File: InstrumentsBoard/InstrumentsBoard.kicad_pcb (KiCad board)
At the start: 2 copper layers, 105.7 x 47.1 mm, 24 parts, among them J1 RJ45_LED_Shielded, Q1 BSS138, Q2 BSS138, U1 Teensy4.1_DEV-16771, U2 OKI

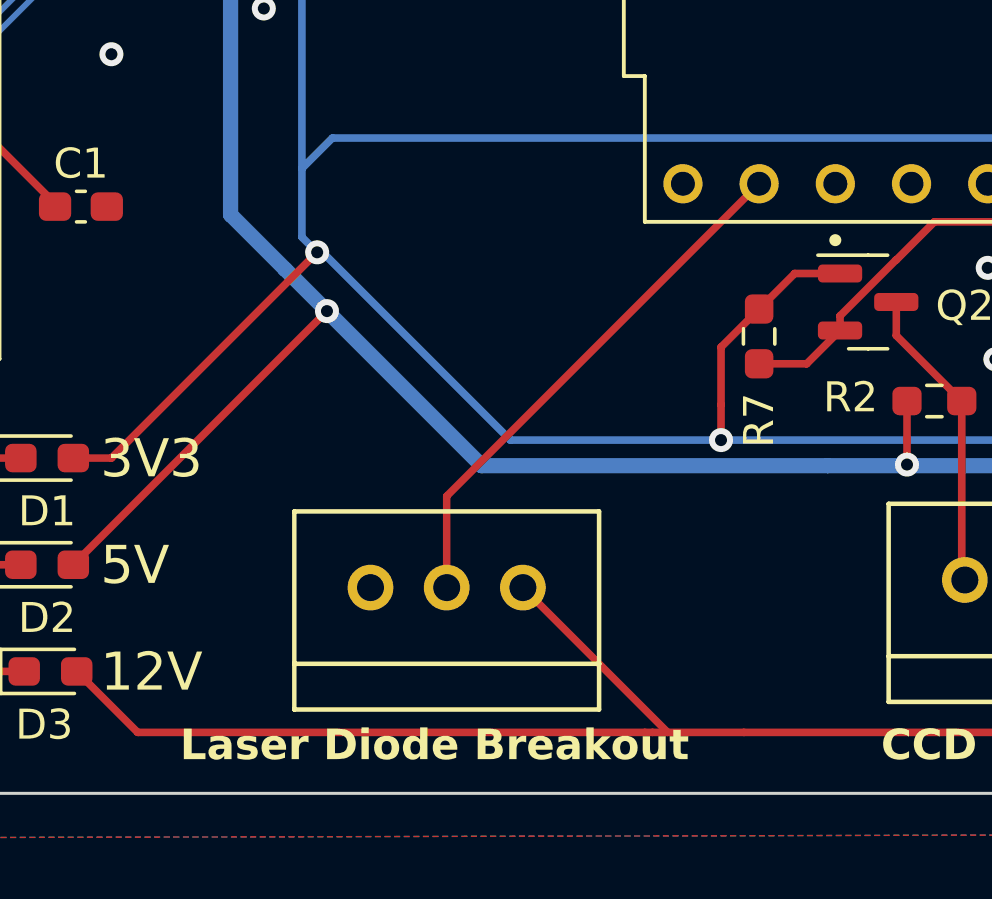
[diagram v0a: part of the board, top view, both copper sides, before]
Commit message: Revert "revert back to laser diode board"
This reverts commit 6528700a9c51bf2c3bc149a74fbf2f6639f4022b.
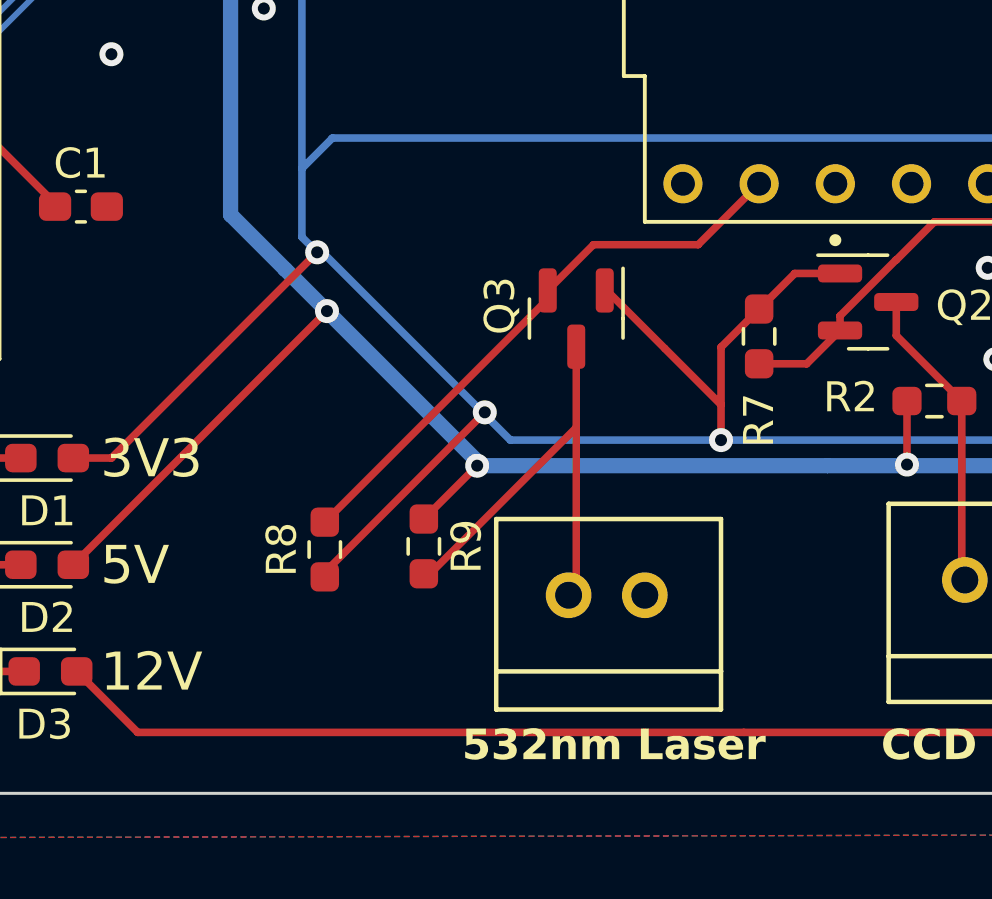
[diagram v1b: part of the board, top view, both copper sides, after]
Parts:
- removed Conn3: Molex_SL_03, MRDT_Connectors:MOLEX_SL_03_Vertical
- added Conn5: Molex_SL_02, MRDT_Connectors:MOLEX_SL_02_Vertical, F.Cu at (67.3, 67.3)
- added Q3: BSS138BK, Package_TO_SOT_SMD:SOT-23, F.Cu at (65.0, 58.1)
- added R8: 4.7k, Resistor_SMD:R_0603_1608Metric_Pad0.98x0.95mm_HandSolder, F.Cu at (56.6, 65.8)
- added R9: 4.7k, Resistor_SMD:R_0603_1608Metric_Pad0.98x0.95mm_HandSolder, F.Cu at (59.9, 65.7)
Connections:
- U1 pad 0: Green_LED -> Green_Laser_3V3
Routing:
- net Green_Laser_3V3: track 0.00 -> 19.3 mm
- net Green_LED: track 17.8 -> 0.00 mm
- net Green_Laser_5V: track 0.00 -> 15.5 mm
- net +3V3: track 139.7 -> 152.8 mm, vias 3 -> 4
- net +12V: track 94.1 -> 87.3 mm
- net +5V: track 143.8 -> 146.3 mm, vias 4 -> 5
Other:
- board text added: "532nm Laser"
- board text added: "5V Signal"
- board text removed: "Laser Diode Breakout"

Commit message: revert back to laser diode board
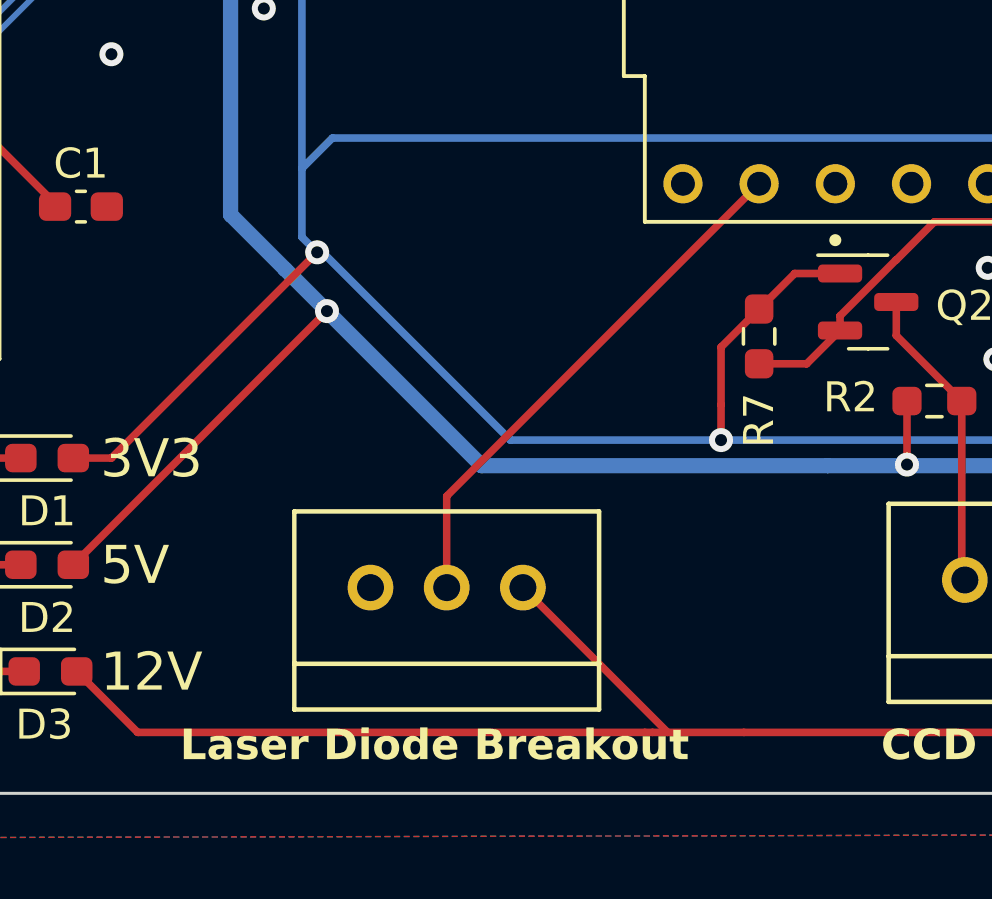
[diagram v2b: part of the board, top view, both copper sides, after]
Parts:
- removed Conn5: Molex_SL_02, MRDT_Connectors:MOLEX_SL_02_Vertical
- removed Q3: BSS138BK, Package_TO_SOT_SMD:SOT-23
- removed R8, R9: 4.7k, Resistor_SMD:R_0603_1608Metric_Pad0.98x0.95mm_HandSolder
- added Conn3: Molex_SL_03, MRDT_Connectors:MOLEX_SL_03_Vertical, F.Cu at (63.2, 67.1)
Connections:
- U1 pad 0: Green_Laser_3V3 -> Green_LED
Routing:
- net Green_Laser_3V3: track 19.3 -> 0.00 mm
- net Green_LED: track 0.00 -> 17.8 mm
- net Green_Laser_5V: track 15.5 -> 0.00 mm
- net +3V3: track 152.8 -> 139.7 mm, vias 4 -> 3
- net +12V: track 87.3 -> 94.1 mm
- net +5V: track 146.3 -> 143.8 mm, vias 5 -> 4
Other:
- board text added: "Laser Diode Breakout"
- board text removed: "532nm Laser"
- board text removed: "5V Signal"
